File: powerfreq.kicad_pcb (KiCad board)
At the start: 2 copper layers, 177.8 x 50.8 mm, 22 parts, among them P1 CONN_01X02, Q1 2N3904, Q2 2N3904

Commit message: add picPET chip and SMA connector
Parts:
- added IC1: picPET-03, Housings_DIP:DIP-8_W7.62mm_LongPads, F.Cu at (184.2, 92.7)
- added J1: SMA, SMA_EDGE:SMA_EDGE, F.Cu at (153.7, 64.8)
- added P2: CONN_01X04, Pin_Headers:Pin_Header_Straight_1x04, F.Cu at (176.5, 76.2)
- P1: value CONN_01X02 -> CONN_01X03; footprint Pin_Headers:Pin_Header_Straight_1x02 -> Connect:Banana_Jack_3Pin
- moved P1 89.2 mm to (78.7, 96.5)
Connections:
- net Net-(C2-Pad2) renamed CLAMP
- net Net-(Q1-Pad3) renamed TRIG
- P1 pad 1: +5V -> Net-(P1-Pad1)
- P1 pad 2: GND -> Net-(P1-Pad2)
- TR1 pad 1: Net-(TR1-Pad1) -> Net-(P1-Pad1)
- TR1 pad 5: Net-(TR1-Pad5) -> Net-(P1-Pad2)

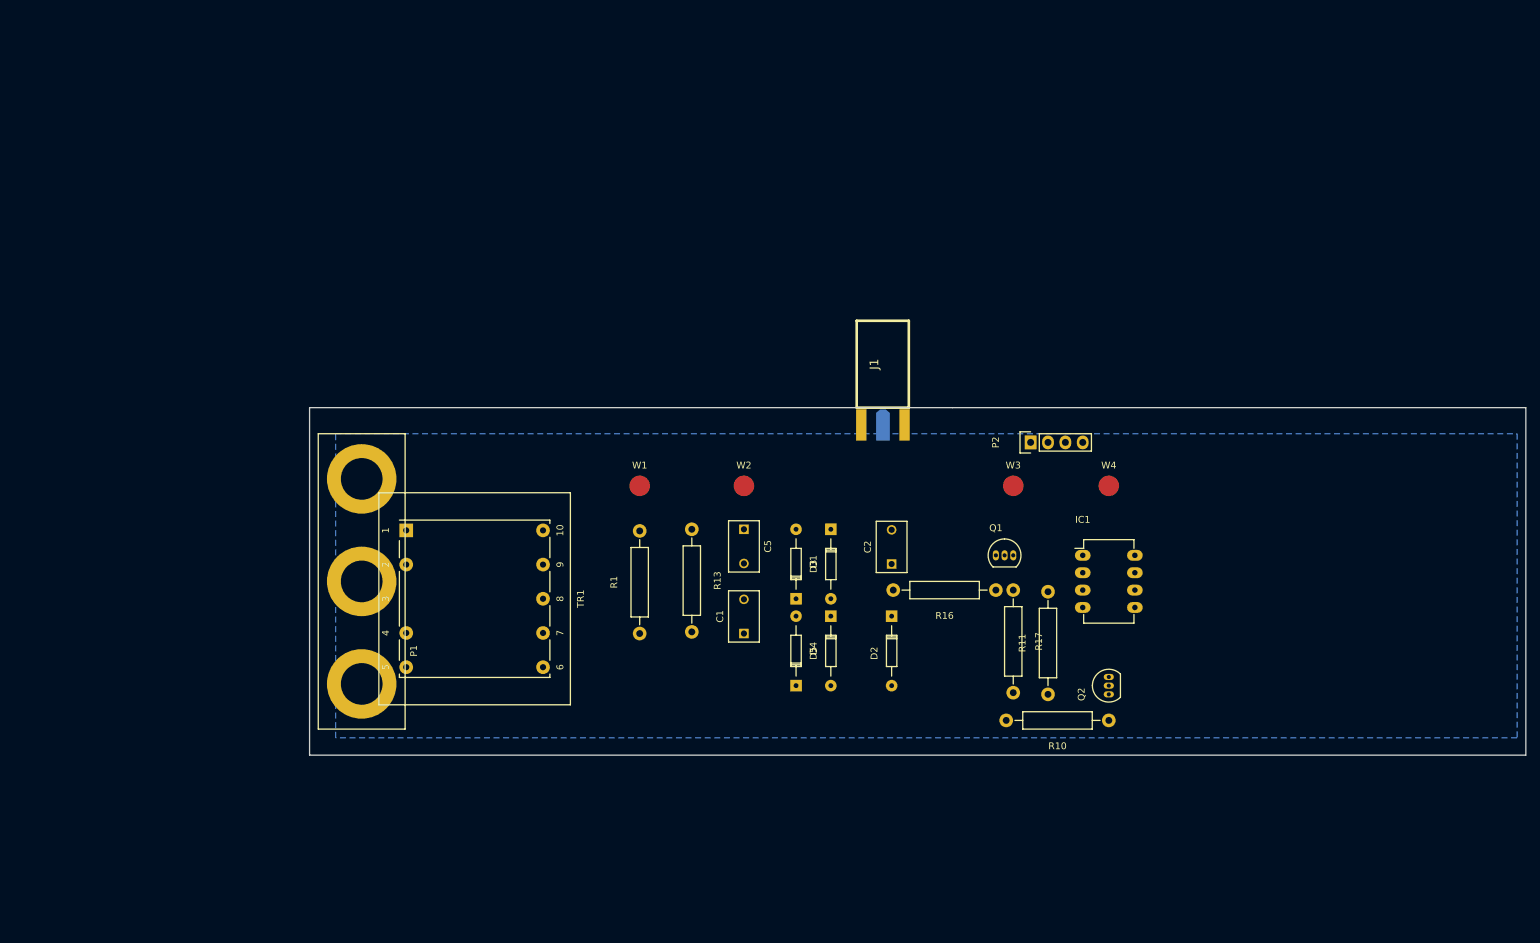
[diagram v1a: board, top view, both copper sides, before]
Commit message: Beginnings of proper layout, new footprints for transformer and picPET.
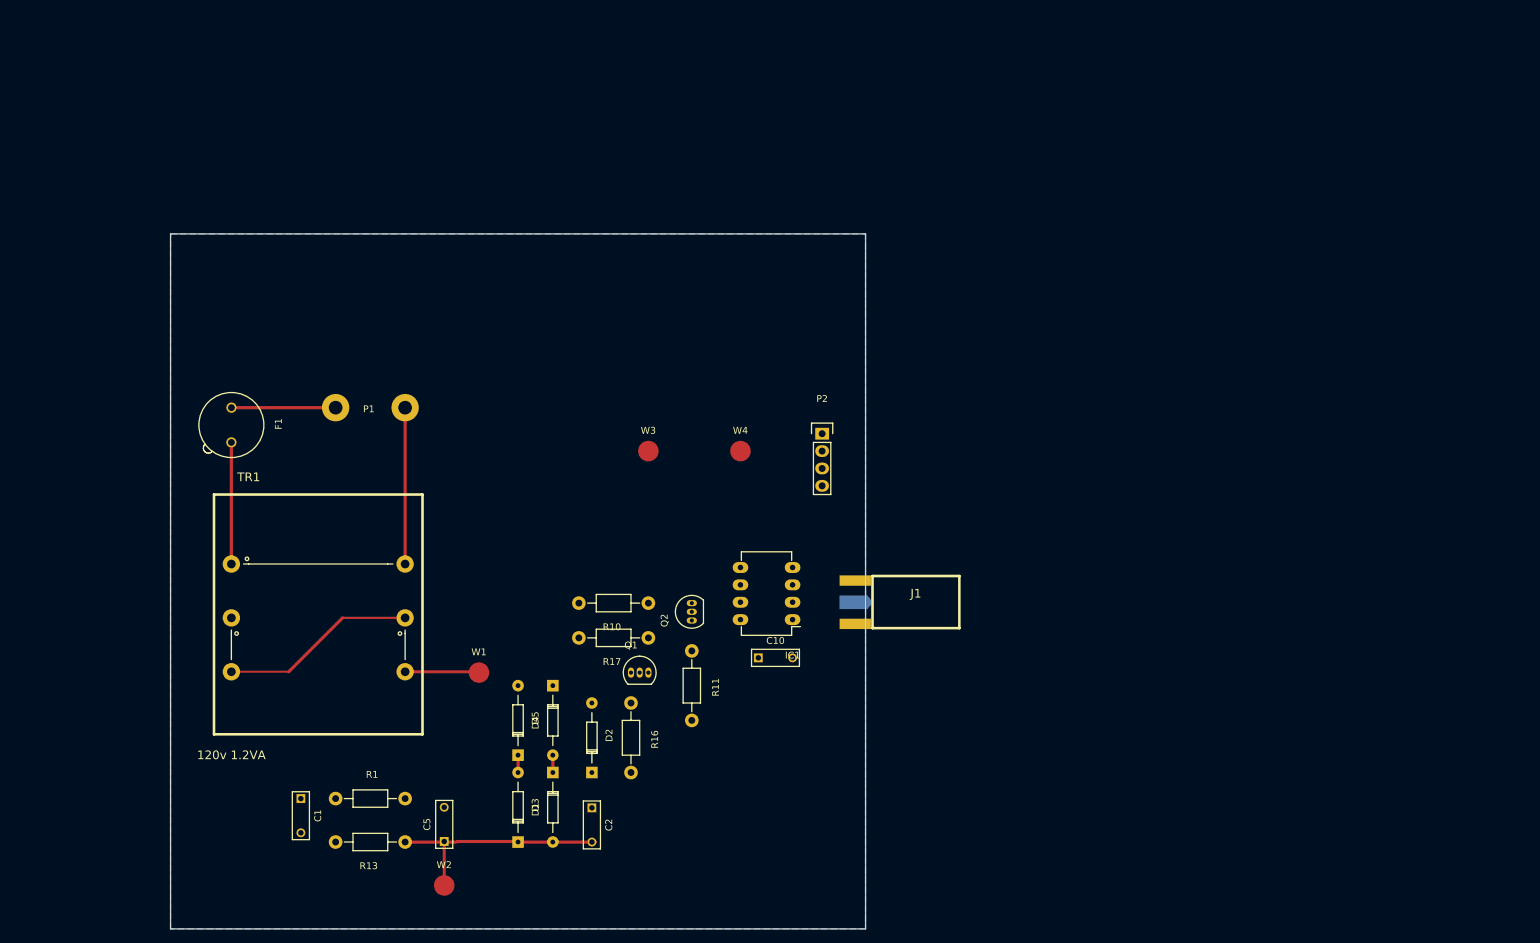
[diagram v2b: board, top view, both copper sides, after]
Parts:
- added C10: 100nF, Capacitors_ThroughHole:C_Rect_L7_W2.5_P5, F.Cu at (136.7, 107.7)
- added F1: 50mA, Fuse_Holders_and_Fuses:Fuseholder_Fuse_TR5_Littlefuse-No560_No460, F.Cu at (59.7, 73.7)
- C1, C2, C5: footprint Capacitors_ThroughHole:C_Disc_D7.5_P5 -> Capacitors_ThroughHole:C_Rect_L7_W2.5_P5
- P1: footprint Connect:Banana_Jack_3Pin -> Wire_Connections_Bridges:WireConnection_2.00mmDrill
- R1, R10, R11, R13, R16, R17: footprint Resistors_ThroughHole:Resistor_Horizontal_RM15mm -> Resistors_ThroughHole:Resistor_Horizontal_RM10mm
- TR1: value 120v 1.5VA -> 120v 1.2VA; footprint Divers:TEZ-28x33 -> transformers-hammond:161E120
- moved W2 73.0 mm to (90.8, 141.0)
- moved R10 69.5 mm to (120.7, 99.7)
- moved C1 69.1 mm to (69.8, 128.3), turned to 270 degrees
- moved D3 64.7 mm to (101.6, 134.6), turned to 90 degrees
- moved C5 63.3 mm to (90.8, 134.5), turned to 90 degrees
- moved R13 62.0 mm to (85.1, 134.6), turned to 180 degrees
- moved Q2 61.9 mm to (127.0, 102.2)
- moved C2 56.5 mm to (112.4, 129.6), turned to 270 degrees
- moved Q1 56.0 mm to (118.1, 109.9)
- moved R16 55.8 mm to (118.1, 114.3), turned to 270 degrees
- moved W4 54.1 mm to (134.1, 77.5)
- moved R17 53.8 mm to (120.7, 104.8), turned to 180 degrees
- moved W3 53.6 mm to (120.7, 77.5)
- moved R11 52.5 mm to (127.0, 106.7), turned to 270 degrees
- moved R1 50.6 mm to (74.9, 128.3), turned to 0 degrees
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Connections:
- P1 pad 1: Net-(P1-Pad1) -> Net-(F1-Pad1)
- TR1 pad 1: Net-(P1-Pad1) -> Net-(F1-Pad2)
- TR1 pad 2: (no net) -> Net-(P1-Pad2)
- TR1 pad 4: (no net) -> Net-(TR1-Pad4)
- TR1 pad 5: Net-(P1-Pad2) -> Net-(TR1-Pad4)
- TR1 pad 6: GND -> Net-(R1-Pad2)
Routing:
- net CLAMP: track 0.00 -> 34.2 mm
- net Net-(TR1-Pad4): track 0.00 -> 28.7 mm
- net Net-(P1-Pad2): track 0.00 -> 22.9 mm
- net Net-(F1-Pad2): track 0.00 -> 17.8 mm
- net Net-(F1-Pad1): track 0.00 -> 15.2 mm
- net Net-(R1-Pad2): track 0.00 -> 11.2 mm
- net Net-(D3-Pad2): track 0.00 -> 2.54 mm
- net Net-(D1-Pad1): track 0.00 -> 2.54 mm
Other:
- board size 177.8 x 50.8 mm -> 101.6 x 101.6 mm

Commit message: Set up layout for Hammond RL6335 box, add FTDI daughter board, and footprint fixups.
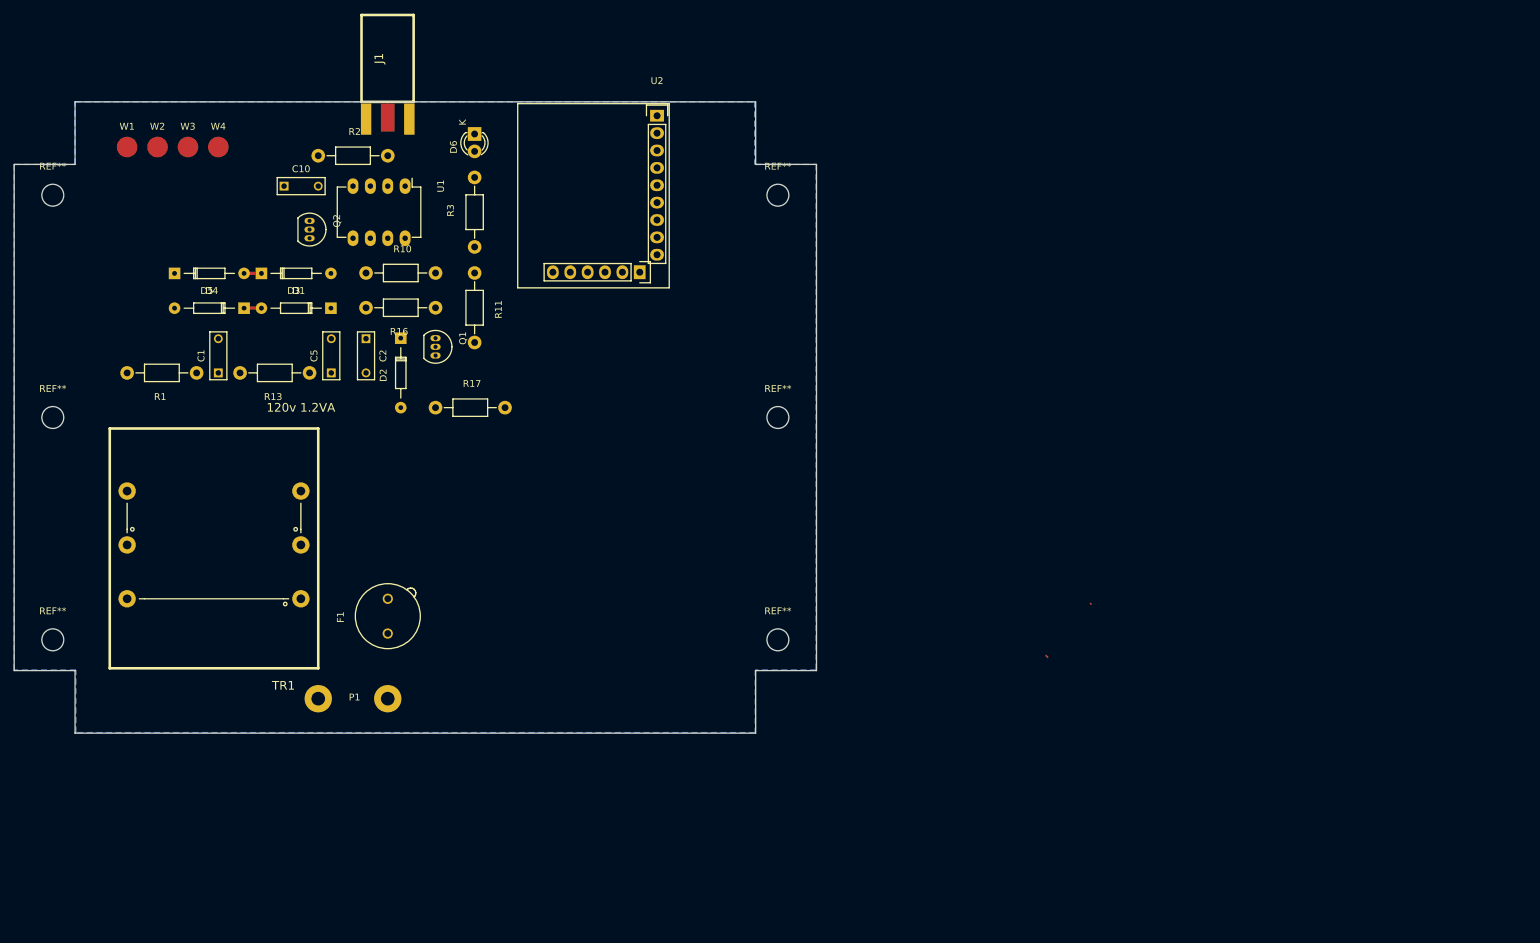
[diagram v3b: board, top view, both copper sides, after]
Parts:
- removed IC1: picPET-03, Housings_DIP:DIP-8_W7.62mm_LongPads
- removed P2: CONN_01X04, Pin_Headers:Pin_Header_Straight_1x04
- added D6: LED, LEDs:LED-3MM, F.Cu at (95.2, 31.1)
- added R2: 51, Resistors_ThroughHole:Resistor_Horizontal_RM10mm, F.Cu at (72.4, 34.3)
- added R3: 1k, Resistors_ThroughHole:Resistor_Horizontal_RM10mm, F.Cu at (95.2, 47.6)
- added REF**: MountingHole_3.2mm_M3, Mounting_Holes:MountingHole_3.2mm_M3, F.Cu at (139.6, 105.1)
- added REF**: MountingHole_3.2mm_M3, Mounting_Holes:MountingHole_3.2mm_M3, F.Cu at (139.6, 72.6)
- added REF**: MountingHole_3.2mm_M3, Mounting_Holes:MountingHole_3.2mm_M3, F.Cu at (33.6, 105.1)
- added REF**: MountingHole_3.2mm_M3, Mounting_Holes:MountingHole_3.2mm_M3, F.Cu at (33.6, 72.6)
- added REF**: MountingHole_3.2mm_M3, Mounting_Holes:MountingHole_3.2mm_M3, F.Cu at (139.6, 40.1)
- added REF**: MountingHole_3.2mm_M3, Mounting_Holes:MountingHole_3.2mm_M3, F.Cu at (33.6, 40.1)
- added U1: picPET-03, Housings_DIP:DIP-8_W7.62mm_LongPads, F.Cu at (85.1, 38.7)
- added U2: MIKROE-483, mikroe:mikroe-483, F.Cu at (123.7, 26.7)
- moved W2 115.8 mm to (48.9, 33.0)
- moved J1 110.8 mm to (81.3, 20.1), turned to 90 degrees
- moved C10 97.8 mm to (67.4, 38.7)
- moved W1 92.5 mm to (44.5, 33.0)
- moved W4 88.3 mm to (57.8, 33.0)
- moved D1 84.5 mm to (64.1, 51.5), turned to 0 degrees
- moved D3 82.7 mm to (74.2, 56.6), turned to 180 degrees
- moved D4 81.8 mm to (51.4, 51.5), turned to 0 degrees
- moved Q2 80.8 mm to (71.1, 43.8), turned to 270 degrees
- moved W3 80.7 mm to (53.3, 33.0)
- moved D5 76.6 mm to (61.5, 56.6), turned to 180 degrees
- moved C2 76.1 mm to (79.4, 61.0)
- moved C5 70.5 mm to (74.3, 66.0)
- moved R13 70.0 mm to (71.1, 66.0)
- moved D2 69.4 mm to (84.5, 61.0), turned to 270 degrees
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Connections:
- net +5V renamed +3V3
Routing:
- net CLAMP: track 34.2 -> 0.11 mm
- net Net-(TR1-Pad4): track 28.7 -> 0.00 mm
- net Net-(P1-Pad2): track 22.9 -> 0.00 mm
- net Net-(F1-Pad2): track 17.8 -> 0.00 mm
- net Net-(F1-Pad1): track 15.2 -> 0.00 mm
- net Net-(R1-Pad2): track 11.2 -> 0.34 mm
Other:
- board size 101.6 x 101.6 mm -> 117.3 x 92.3 mm

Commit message: New layout, power on top, I/O on right side
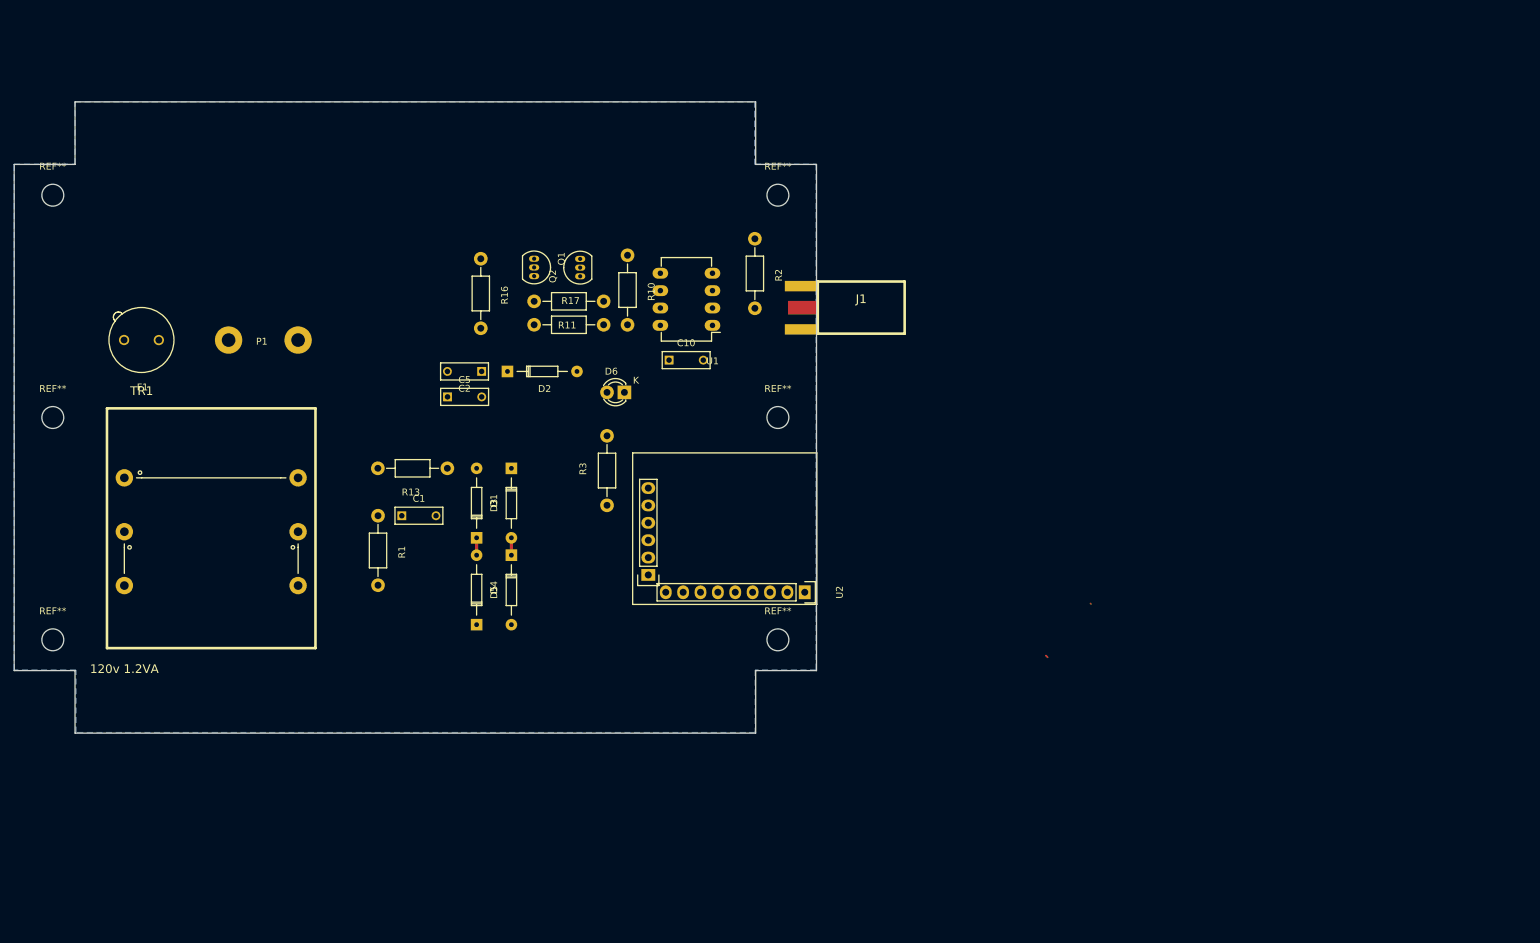
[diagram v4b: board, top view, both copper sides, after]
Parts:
- removed W1, W2, W3, W4: TEST_1P, Measurement_Points:Measurement_Point_Round-SMD-Pad_Big
- moved J1 78.8 mm to (151.8, 55.2), turned to 0 degrees
- moved U2 76.3 mm to (145.3, 99.9), turned to 180 degrees
- moved D4 67.7 mm to (95.5, 102.8), turned to 90 degrees
- moved R2 65.0 mm to (136.2, 46.4), turned to 270 degrees
- moved C10 61.8 mm to (123.7, 64.2)
- moved P1 57.4 mm to (59.3, 61.2), turned to 0 degrees
- moved F1 54.1 mm to (46.5, 61.2), turned to 180 degrees
- moved D5 53.2 mm to (100.6, 92.7), turned to 270 degrees
- moved D1 49.8 mm to (95.5, 90.1), turned to 90 degrees
- moved U1 49.3 mm to (130.0, 59.1), turned to 180 degrees
- moved TR1 49.0 mm to (41.5, 71.2), turned to 0 degrees
- moved D6 43.7 mm to (117.1, 68.9), turned to 180 degrees
- moved R3 42.4 mm to (114.6, 85.4)
- moved Q2 40.4 mm to (110.7, 51.9), turned to 90 degrees
- moved R10 38.3 mm to (117.6, 48.8), turned to 270 degrees
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
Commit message: Add track routing, and a few other fixups.
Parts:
- moved D6 12.0 mm to (109.1, 77.8), turned to 90 degrees
- moved C10 1.38 mm to (125.0, 63.9)
- moved R16 0.10 mm to (96.3, 49.4)
- moved R2 0.06 mm to (136.3, 46.4)
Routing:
- net +3V3: track 0.00 -> 70.2 mm
- net Net-(D6-Pad1): track 0.00 -> 54.8 mm
- net SERIAL_RX: track 0.00 -> 45.3 mm, vias 0 -> 4
- net Net-(TR1-Pad4): track 0.00 -> 28.7 mm
- net CLAMP: track 0.11 -> 23.6 mm
- net Net-(F1-Pad2): track 0.00 -> 20.2 mm
- net Net-(P1-Pad2): track 0.00 -> 20.1 mm
- net 10MHz: track 0.00 -> 13.1 mm
- net 60PPS: track 0.00 -> 13.0 mm
- net Net-(R1-Pad2): track 0.00 -> 11.7 mm
- net Net-(C1-Pad1): track 0.00 -> 10.4 mm
- net Net-(F1-Pad1): track 0.00 -> 10.2 mm
- net Net-(C2-Pad1): track 0.00 -> 10.1 mm
- net Net-(Q1-Pad1): track 0.00 -> 7.70 mm
- net TRIG: track 0.00 -> 7.11 mm
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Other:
- rule trace_min: 0.2 -> 0.1524
